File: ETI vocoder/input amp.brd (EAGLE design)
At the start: 52.4 x 37.5 mm, 32 parts, among them IC1 LM4558N, IC2 LM1458N

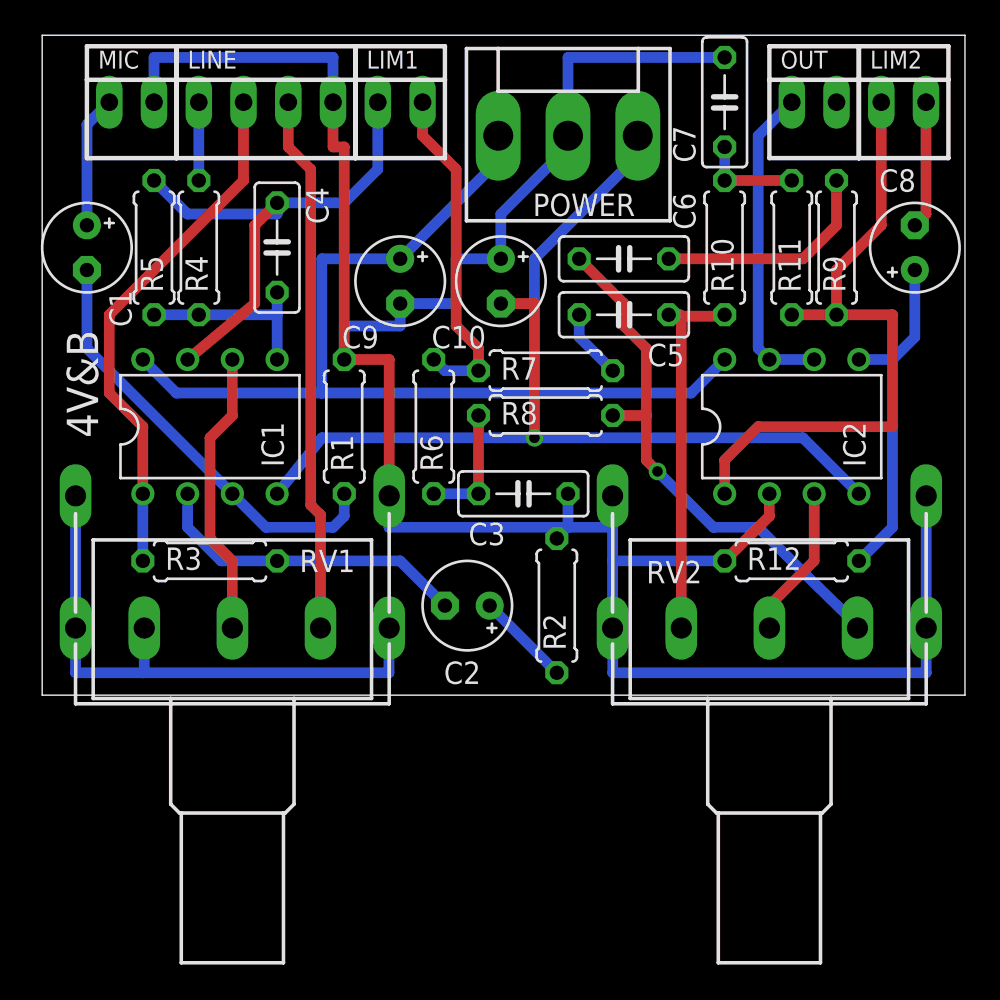
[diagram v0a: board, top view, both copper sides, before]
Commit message: All ETI boards checked for caps and pots
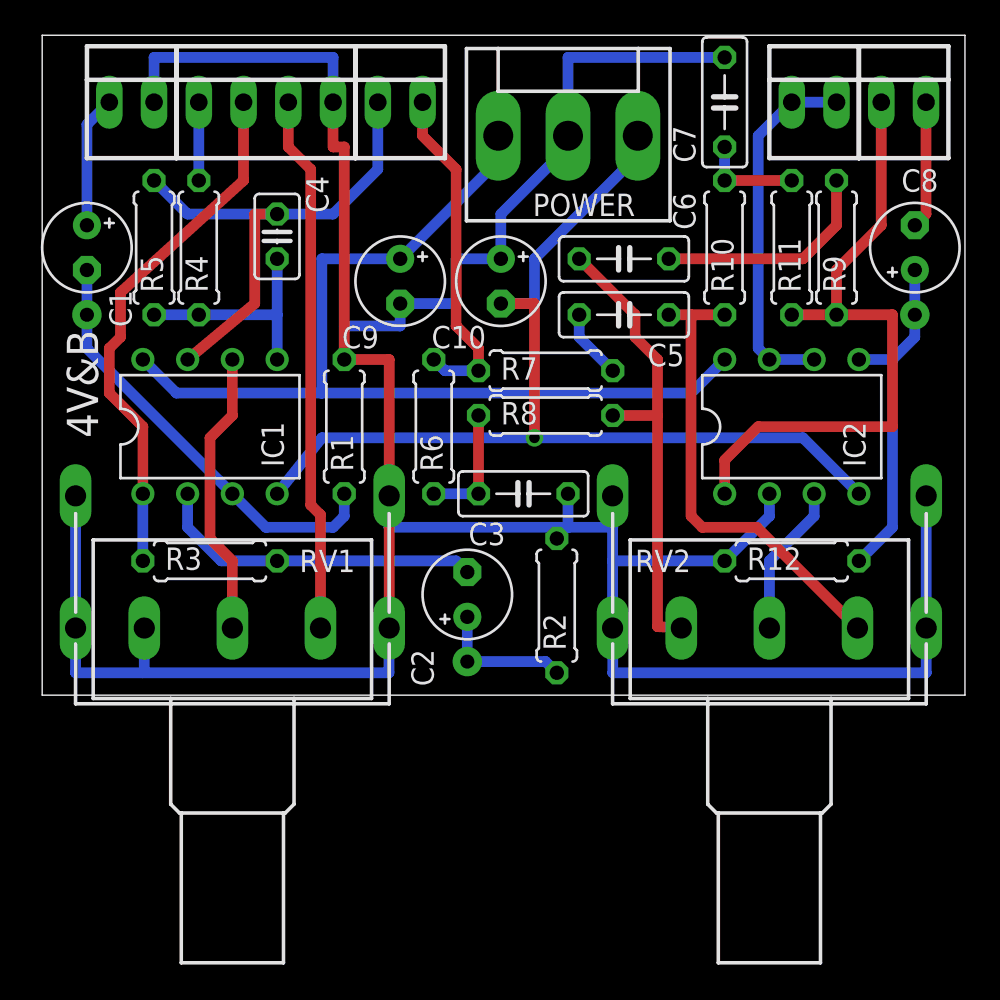
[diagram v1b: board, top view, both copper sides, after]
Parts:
- C4: device resistor:C050-025X075 -> resistor:C025-025X050
- R8: value (none) -> 47k
- moved C4 0.64 mm to (13.3, 26.0)
- moved C2 0.63 mm to (24.1, 5.71), turned to 90 degrees
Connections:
- net N$10: now also RV2.1E; no longer RV2.1A
- net N$9: now also RV2.1A; no longer RV2.1E
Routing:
- net GND: track 176.3 -> 183.8 mm
- net N$10: track 20.9 -> 26.7 mm
- net N$9: track 31.0 -> 26.6 mm, vias 1 -> 0
- net OUT: track 18.2 -> 20.7 mm
- net N$4: track 5.39 -> 7.88 mm
- net N$6: track 10.8 -> 12.7 mm
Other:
- board text added: "+12V"
- board text added: "-12V"
- board text added: "Amp out"
- board text added: "From mic"
- board text added: "GND"
- board text added: "In"
- board text added: "Lim"
- board text added: "Lim 1"
- board text added: "Lim ret"
- board text added: "Line"
- board text added: "Mic"
- board text added: "Out"
- board text added: "Tone out"
- board text added: "gnd"
- board text added: "ret"
- board text added: "sw gnd"

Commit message: Finished first of two halves of the universal voice board
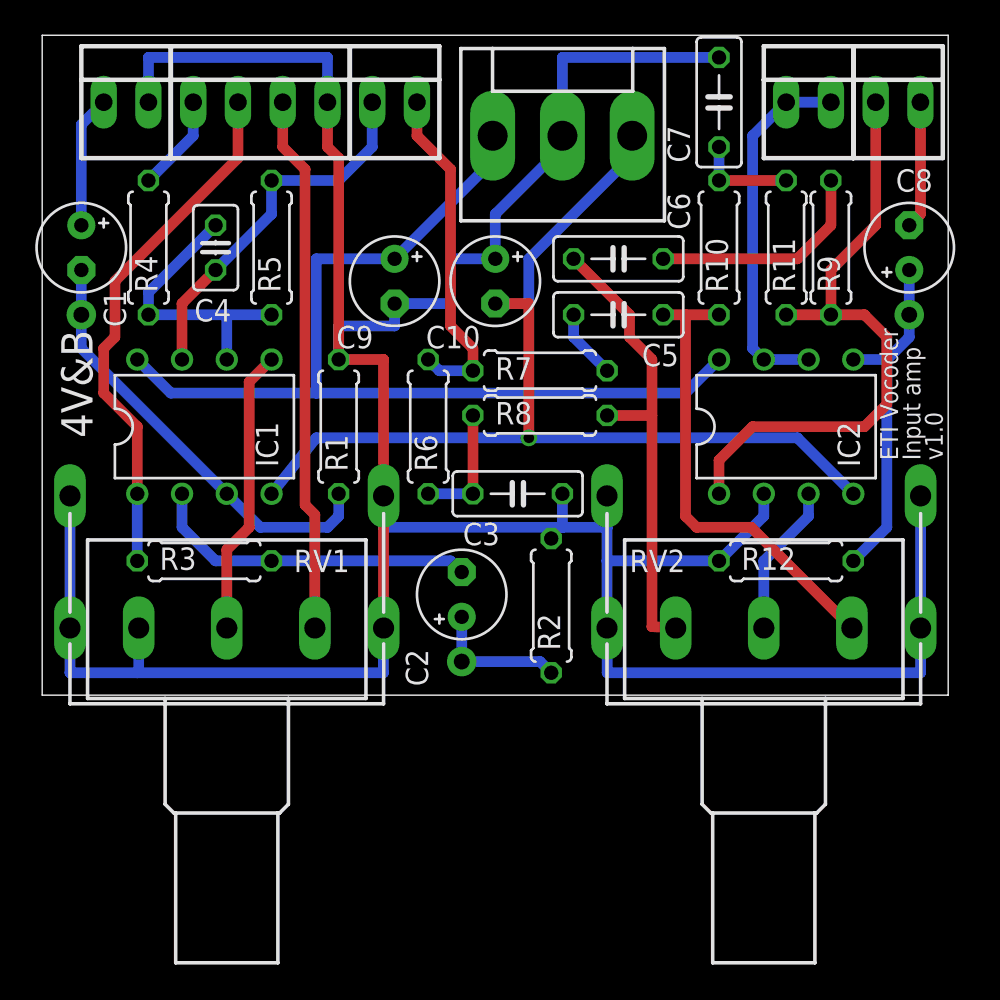
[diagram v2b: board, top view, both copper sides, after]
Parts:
- moved R5 6.67 mm to (13.0, 25.4)
- moved C4 3.55 mm to (9.84, 25.4), turned to 270 degrees
- moved R4 2.86 mm to (6.03, 25.4)
- moved C5 0.32 mm to (32.7, 21.6)
- moved C6 0.32 mm to (32.7, 24.8)
- moved C7 0.32 mm to (38.4, 33.7)
- moved C8 0.32 mm to (49.2, 25.4)
- moved IC2 0.32 mm to (42.2, 15.2)
- moved LIM2 0.32 mm to (48.6, 33.7)
- moved R10 0.32 mm to (38.4, 25.4)
- moved R11 0.32 mm to (42.2, 25.4)
- moved R12 0.32 mm to (42.2, 7.62)
- moved R2 0.32 mm to (28.9, 5.08)
- moved R6 0.32 mm to (21.9, 15.2)
- moved R9 0.32 mm to (44.8, 25.4)
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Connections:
- net N$5: now also IC1.5; no longer IC1.6
- net N$6: now also IC1.6; no longer IC1.5
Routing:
- net AMP_OUT: track 29.7 -> 21.3 mm
- net N$6: track 12.7 -> 16.2 mm
- net TONE_OUT: track 37.4 -> 35.9 mm
- net SWITCHED_GND: track 4.45 -> 5.50 mm
- net N$17: vias 0 -> 1
- net N$4: vias 0 -> 1
- net N$1: vias 0 -> 1
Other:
- board size 52.4 x 37.5 mm -> 51.4 x 37.5 mm
- board text added: "ETI Vocoder"
- board text added: "Input amp"
- board text added: "v1.0"
